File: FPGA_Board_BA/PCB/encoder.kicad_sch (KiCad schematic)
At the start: 1 part, among them J1101 Molex_Mini_Fit_Jr_2x08pin

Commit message: Besprechung mit Leo
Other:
- note added: "3 Phasen kommen auch vom gleichen Stecker, muss man vllt noch ändern JST Xh oder VH könnte hier bequem sein oder s04b-xask JST"
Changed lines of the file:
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@@
 	(generator_version "9.0")
 	(paper "A4")
+	(text "3 Phasen kommen auch vom gleichen Stecker, muss man vllt noch ändern\nJST Xh oder VH könnte hier bequem sein\noder s04b-xask JST"
+		(exclude_from_sim no)
+		(at 185.928 35.814 0)
+		(effects
+			(font
+				(size 1.27 1.27)
+			)
+			(justify left)
+		)
+	)
 	(text "(The encoder is not Differential)"
 		(exclude_from_sim no)

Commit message: lots of work
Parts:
- removed J1101: Molex_Mini_Fit_Jr_2x08pin, MYLIB_Misc:Molex_2x8pin_vertical_tht, symbol MYLIB_Misc:Molex_Mini_Fit_Jr_2x08
- added C1806, C1807, C1808, C1809: 100n_0603, WLIB_Capacitor:C_0603, symbol WLIB_C:100n_0603
- added J1801: Molex_Mini_Fit_Jr_2x08pin, MYLIB_Misc:Molex_2x8pin_vertical_tht, symbol MYLIB_Misc:Molex_Mini_Fit_Jr_2x08
- added U1802, U1803: SN74LXC2T45Q1, MYLIB_Misc:SN74LXC2T45QDCURQ1, symbol MYLIB_Misc:SN74LXC2T45Q1
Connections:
- net +5V: now also C1807.2, C1808.2, J1801.12 (Pin_12), U1802.1 (VCCA), U1802.5 (DIR), U1803.1 (VCCA), U1803.5 (DIR)
- net ENC_A: now also U1802.7 (B1)
- net ENC_B: now also U1802.6 (B2)
- net ENC_I: now also U1803.7 (B1)
- net GND: now also C1806.2, C1807.1, C1808.1, C1809.2, J1801.7 (Pin_7), U1802.4 (GND), U1803.4 (GND)
- new net +3.3V: C1806.1, C1809.1, U1802.8 (VCCB), U1803.8 (VCCB)
- new net ENC_A_5V: J1801.15 (Pin_15), U1802.2 (A1)
- new net ENC_B_5V: J1801.14 (Pin_14), U1802.3 (A2)
- new net ENC_I_5V: J1801.13 (Pin_13), U1803.2 (A1)
- new net M_PHA: J1801.9 (Pin_9)
- new net M_PHB: J1801.10 (Pin_10)
- new net M_PHC: J1801.11 (Pin_11)
- no-connect marks 11 -> 10

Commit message: work
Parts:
- renumbered C1808 to C72, C1807 to C73, C1809 to C74, C1806 to C75, J1801 to J20, U1802 to U16, U1803 to U17
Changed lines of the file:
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@@
 		(dnp no)
 		(fields_autoplaced yes)
-		(property "Reference" "#PWR01815"
+		(property "Reference" "#PWR099"
 			(at 251.46 130.81 0)
 			(effects
@@
 			(project "FPGA_Board_BA"
 				(path "/fd7503bc-e7fc-4766-b224-3d1c3d7de5ff/81c9b981-9c9c-474d-998d-986f60c2f16d"
-					(reference "#PWR01815")
+					(reference "#PWR099")
 					(unit 1)
 				)
@@
 		(dnp no)
 		(fields_autoplaced yes)
-		(property "Reference" "#PWR01817"
+		(property "Reference" "#PWR0100"
 			(at 254 87.63 0)
 			(effects
@@
 			(project "FPGA_Board_BA"
 				(path "/fd7503bc-e7fc-4766-b224-3d1c3d7de5ff/81c9b981-9c9c-474d-998d-986f60c2f16d"
-					(reference "#PWR01817")
+					(reference "#PWR0100")
 					(unit 1)
 				)
@@
 		(dnp no)
 		(fields_autoplaced yes)
-		(property "Reference" "#PWR01813"
+		(property "Reference" "#PWR090"
 			(at 187.96 144.78 0)
 			(effects
@@
 			(project "FPGA_Board_BA"
 				(path "/fd7503bc-e7fc-4766-b224-3d1c3d7de5ff/81c9b981-9c9c-474d-998d-986f60c2f16d"
-					(reference "#PWR01813")
+					(reference "#PWR090")
 					(unit 1)
 				)
@@
 		(dnp no)
 		(fields_autoplaced yes)
-		(property "Reference" "U1802"
+		(property "Reference" "U16"
 			(at 221.8533 104.14 0)
 			(effects
@@
 			(project ""
 				(path "/fd7503bc-e7fc-4766-b224-3d1c3d7de5ff/81c9b981-9c9c-474d-998d-986f60c2f16d"
-					(reference "U1802")
+					(reference "U16")
 					(unit 1)
 				)
@@
 		(dnp no)
 		(fields_autoplaced yes)
-		(property "Reference" "#PWR01808"
+		(property "Reference" "#PWR095"
 			(at 219.71 113.03 0)
 			(effects
@@
 			(project ""
 				(path "/fd7503bc-e7fc-4766-b224-3d1c3d7de5ff/81c9b981-9c9c-474d-998d-986f60c2f16d"
-					(reference "#PWR01808")
+					(reference "#PWR095")
 					(unit 1)
 				)
@@
 		(dnp no)
 		(fields_autoplaced yes)
-		(property "Reference" "C1806"
+		(property "Reference" "C75"
 			(at 243.84 111.76 90)
 			(effects
@@
 			(project ""
 				(path "/fd7503bc-e7fc-4766-b224-3d1c3d7de5ff/81c9b981-9c9c-474d-998d-986f60c2f16d"
-					(reference "C1806")
+					(reference "C75")
 					(unit 1)
 				)
@@
 		(dnp no)
 		(fields_autoplaced yes)
-		(property "Reference" "#PWR01816"
+		(property "Reference" "#PWR089"
 			(at 187.96 86.36 0)
 			(effects
@@
 			(project "FPGA_Board_BA"
 				(path "/fd7503bc-e7fc-4766-b224-3d1c3d7de5ff/81c9b981-9c9c-474d-998d-986f60c2f16d"
-					(reference "#PWR01816")
+					(reference "#PWR089")
 					(unit 1)
 				)
@@
 		(dnp no)
 		(fields_autoplaced yes)
-		(property "Reference" "U1803"
+		(property "Reference" "U17"
 			(at 221.8533 147.32 0)
 			(effects
@@
 			(project "FPGA_Board_BA"
 				(path "/fd7503bc-e7fc-4766-b224-3d1c3d7de5ff/81c9b981-9c9c-474d-998d-986f60c2f16d"
-					(reference "U1803")
+					(reference "U17")
 					(unit 1)
 				)
@@
 		(dnp no)
 		(fields_autoplaced yes)
-		(property "Reference" "#PWR01812"
+		(property "Reference" "#PWR091"
 			(at 189.23 100.33 0)
 			(effects
@@
 			(project "FPGA_Board_BA"
 				(path "/fd7503bc-e7fc-4766-b224-3d1c3d7de5ff/81c9b981-9c9c-474d-998d-986f60c2f16d"
-					(reference "#PWR01812")
+					(reference "#PWR091")
 					(unit 1)
 				)
@@
 		(dnp no)
 		(fields_autoplaced yes)
-		(property "Reference" "#PWR01814"
+		(property "Reference" "#PWR092"
 			(at 190.5 129.54 0)
 			(effects
@@
 			(project "FPGA_Board_BA"
 				(path "/fd7503bc-e7fc-4766-b224-3d1c3d7de5ff/81c9b981-9c9c-474d-998d-986f60c2f16d"
-					(reference "#PWR01814")
+					(reference "#PWR092")
 					(unit 1)
 				)
@@
 		(dnp no)
 		(fields_autoplaced yes)
-		(property "Reference" "J1801"
+		(property "Reference" "J20"
 			(at 220.98 30.48 0)
 			(effects
@@
 			(project ""
 				(path "/fd7503bc-e7fc-4766-b224-3d1c3d7de5ff/81c9b981-9c9c-474d-998d-986f60c2f16d"
-					(reference "J1801")
+					(reference "J20")
 					(unit 1)
 				)
@@
 		(dnp no)
 		(fields_autoplaced yes)
-		(property "Reference" "#PWR01810"
+		(property "Reference" "#PWR096"
 			(at 219.71 157.48 0)
 			(effects
@@
 			(project "FPGA_Board_BA"
 				(path "/fd7503bc-e7fc-4766-b224-3d1c3d7de5ff/81c9b981-9c9c-474d-998d-986f60c2f16d"
-					(reference "#PWR01810")
+					(reference "#PWR096")
 					(unit 1)
 				)
@@
 		(dnp no)
 		(fields_autoplaced yes)
-		(property "Reference" "#PWR01811"
+		(property "Reference" "#PWR097"
 			(at 226.06 121.92 0)
 			(effects
@@
 			(project "FPGA_Board_BA"
 				(path "/fd7503bc-e7fc-4766-b224-3d1c3d7de5ff/81c9b981-9c9c-474d-998d-986f60c2f16d"
-					(reference "#PWR01811")
+					(reference "#PWR097")
 					(unit 1)
 				)
@@
 		(dnp no)
 		(fields_autoplaced yes)
-		(property "Reference" "C1807"
+		(property "Reference" "C73"
 			(at 199.39 111.76 90)
 			(effects
@@
 			(project "FPGA_Board_BA"
 				(path "/fd7503bc-e7fc-4766-b224-3d1c3d7de5ff/81c9b981-9c9c-474d-998d-986f60c2f16d"
-					(reference "C1807")
+					(reference "C73")
 					(unit 1)
 				)
@@
 		(dnp no)
 		(fields_autoplaced yes)
-		(property "Reference" "#PWR01806"
+		(property "Reference" "#PWR093"
 			(at 210.82 78.74 0)
 			(effects
@@
 			(project "FPGA_Board_BA"
 				(path "/fd7503bc-e7fc-4766-b224-3d1c3d7de5ff/81c9b981-9c9c-474d-998d-986f60c2f16d"
-					(reference "#PWR01806")
+					(reference "#PWR093")
 					(unit 1)
 				)
@@
 		(dnp no)
 		(fields_autoplaced yes)
-		(property "Reference" "C1808"
+		(property "Reference" "C72"
 			(at 198.12 68.58 90)
 			(effects
@@
 			(project "FPGA_Board_BA"
 				(path "/fd7503bc-e7fc-4766-b224-3d1c3d7de5ff/81c9b981-9c9c-474d-998d-986f60c2f16d"
-					(reference "C1808")
+					(reference "C72")
 					(unit 1)
 				)
@@
 		(dnp no)
 		(fields_autoplaced yes)
-		(property "Reference" "#PWR01807"
+		(property "Reference" "#PWR098"
 			(at 228.6 78.74 0)
 			(effects
@@
 			(project ""
 				(path "/fd7503bc-e7fc-4766-b224-3d1c3d7de5ff/81c9b981-9c9c-474d-998d-986f60c2f16d"
-					(reference "#PWR01807")
+					(reference "#PWR098")
 					(unit 1)
 				)
@@
 		(dnp no)
 		(fields_autoplaced yes)
-		(property "Reference" "#PWR01809"
+		(property "Reference" "#PWR094"
 			(at 213.36 121.92 0)
 			(effects
@@
 			(project "FPGA_Board_BA"
 				(path "/fd7503bc-e7fc-4766-b224-3d1c3d7de5ff/81c9b981-9c9c-474d-998d-986f60c2f16d"
-					(reference "#PWR01809")
+					(reference "#PWR094")
 					(unit 1)
 				)
@@
 		(dnp no)
 		(fields_autoplaced yes)
-		(property "Reference" "C1809"
+		(property "Reference" "C74"
 			(at 241.3 68.58 90)
 			(effects
@@
 			(project "FPGA_Board_BA"
 				(path "/fd7503bc-e7fc-4766-b224-3d1c3d7de5ff/81c9b981-9c9c-474d-998d-986f60c2f16d"
-					(reference "C1809")
-					(unit 1)
-				)
+					(reference "C74")
+					(unit 1)
+				)

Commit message: Besprechung mit Leo
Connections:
- net M_PHA: no longer names the net of J20.9 (Pin_9)
- net M_PHB: no longer names the net of J20.10 (Pin_10)
- net M_PHC: no longer names the net of J20.11 (Pin_11)
- no-connect marks 10 -> 13
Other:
- note added: "JST 6 pin für Encoder"
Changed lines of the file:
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@@
 		)
 	)
+	(text "JST 6 pin für Encoder"
+		(exclude_from_sim no)
+		(at 253.492 24.13 0)
+		(effects
+			(font
+				(size 1.27 1.27)
+			)
+		)
+	)
 	(junction
 		(at 219.71 149.86)
@@
 	)
 	(no_connect
+		(at 227.33 36.83)
+	)
+	(no_connect
 		(at 214.63 46.99)
 	)
@@
 	)
 	(no_connect
+		(at 227.33 41.91)
+	)
+	(no_connect
 		(at 229.87 137.16)
 	)
@@
 	)
 	(no_connect
+		(at 227.33 39.37)
+	)
+	(no_connect
 		(at 214.63 36.83)
 	)
@@
 	(wire
 		(pts
-			(xy 227.33 41.91) (xy 233.68 41.91)
-		)
-		(stroke
-			(width 0)
-			(type default)
-		)
-	)
-	(wire
-		(pts
 			(xy 209.55 142.24) (xy 187.96 142.24)
 		)
@@
 	(wire
 		(pts
-			(xy 227.33 36.83) (xy 233.68 36.83)
-		)
-		(stroke
-			(width 0)
-			(type default)
-		)
-	)
-	(wire
-		(pts
 			(xy 217.17 119.38) (xy 217.17 121.92)
 		)
@@
 	(wire
 		(pts
-			(xy 227.33 39.37) (xy 233.68 39.37)
-		)
-		(stroke
-			(width 0)
-			(type default)
-		)
-	)
-	(wire
-		(pts
 			(xy 238.76 52.07) (xy 227.33 52.07)
 		)
@@
 		)
 	)
-	(global_label "M_PHC"
-		(shape bidirectional)
-		(at 233.68 41.91 0)
-		(fields_autoplaced yes)
-		(effects
-			(font
-				(size 1.27 1.27)
-			)
-			(justify left)
-		)
-		(property "Intersheetrefs" "${INTERSHEET_REFS}"
-			(at 244.066 41.91 0)
-			(effects
-				(font
-					(size 1.27 1.27)
-				)
-				(justify left)
-				(hide yes)
-			)
-		)
-	)
-	(global_label "M_PHB"
-		(shape bidirectional)
-		(at 233.68 39.37 0)
-		(fields_autoplaced yes)
-		(effects
-			(font
-				(size 1.27 1.27)
-			)
-			(justify left)
-		)
-		(property "Intersheetrefs" "${INTERSHEET_REFS}"
-			(at 244.066 39.37 0)
-			(effects
-				(font
-					(size 1.27 1.27)
-				)
-				(justify left)
-				(hide yes)
-			)
-		)
-	)
-	(global_label "M_PHA"
-		(shape bidirectional)
-		(at 233.68 36.83 0)
-		(fields_autoplaced yes)
-		(effects
-			(font
-				(size 1.27 1.27)
-			)
-			(justify left)
-		)
-		(property "Intersheetrefs" "${INTERSHEET_REFS}"
-			(at 243.8846 36.83 0)
-			(effects
-				(font
-					(size 1.27 1.27)
-				)
-				(justify left)
-				(hide yes)
-			)
-		)
-	)

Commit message: 22.11
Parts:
- removed C72, C73, C74, C75: 100n_0603, WLIB_Capacitor:C_0603, symbol WLIB_C:100n_0603
- removed J20: Molex_Mini_Fit_Jr_2x08pin, MYLIB_Misc:Molex_2x8pin_vertical_tht, symbol MYLIB_Misc:Molex_Mini_Fit_Jr_2x08
- removed U16, U17: SN74LXC2T45Q1, MYLIB_Misc:SN74LXC2T45QDCURQ1, symbol MYLIB_Misc:SN74LXC2T45Q1
- added J20: JST_XH_05_vertical, Connector_JST:JST_XH_B5B-XH-A_1x05_P2.50mm_Vertical, symbol WLIB_J:JST_XH_05_vertical
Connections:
- net +5V: now also J20.1 (Pin_1)
- net ENC_A_5V: now also J20.5 (Pin_5)
- net ENC_B_5V: now also J20.4 (Pin_4)
- net ENC_I_5V: now also J20.3 (Pin_3)
- net GND: now also J20.2 (Pin_2)
- no-connect marks 13 -> 2
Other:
- added sheet Level Shifter Encoder 1 (ls_encoder.kicad_sch)
- added sheet Level Shifter Encoder 2 (ls_encoder.kicad_sch)
- note added: "JST 5 pin für Encoder"
- note removed: "3 Phasen kommen auch vom gleichen Stecker, muss man vllt noch ändern JST Xh oder VH könnte hier bequem sein oder s04b-xask JST"
- note removed: "JST 6 pin für Encoder"

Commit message: exported stuff
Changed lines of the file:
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@@
 	(rectangle
 		(start 194.31 26.67)
-		(end 247.65 55.88)
+		(end 257.81 55.88)
 		(stroke
 			(width 0)
@@
 		)
 	)
+	(junction
+		(at 231.14 38.1)
+		(diameter 0)
+		(color 0 0 0 0)
+	)
 	(no_connect
 		(at 238.76 102.87)
@@
 	(wire
 		(pts
+			(xy 247.65 41.91) (xy 247.65 40.64)
+		)
+		(stroke
+			(width 0)
+			(type default)
+		)
+	)
+	(wire
+		(pts
 			(xy 190.5 100.33) (xy 209.55 100.33)
 		)
@@
 	(wire
 		(pts
-			(xy 234.95 102.87) (xy 238.76 102.87)
+			(xy 247.65 40.64) (xy 224.79 40.64)
 		)
 		(stroke
@@
 	(wire
 		(pts
-			(xy 224.79 40.64) (xy 238.76 40.64)
+			(xy 234.95 102.87) (xy 238.76 102.87)
 		)
 		(stroke
@@
 	(wire
 		(pts
-			(xy 224.79 38.1) (xy 238.76 38.1)
+			(xy 224.79 38.1) (xy 231.14 38.1)
 		)
 		(stroke
@@
 	(wire
 		(pts
+			(xy 231.14 38.1) (xy 238.76 38.1)
+		)
+		(stroke
+			(width 0)
+			(type default)
+		)
+	)
+	(wire
+		(pts
 			(xy 194.31 85.09) (xy 209.55 85.09)
 		)
@@
 		)
 	)
+	(wire
+		(pts
+			(xy 231.14 34.29) (xy 231.14 38.1)
+		)
+		(stroke
+			(width 0)
+			(type default)
+		)
+	)
 	(image
 		(at 91.44 64.3793)
@@
 	)
 	(symbol
+		(lib_id "power:GND")
+		(at 247.65 41.91 0)
+		(unit 1)
+		(exclude_from_sim no)
+		(in_bom yes)
+		(on_board yes)
+		(dnp no)
+		(fields_autoplaced yes)
+		(property "Reference" "#PWR0285"
+			(at 247.65 48.26 0)
+			(effects
+				(font
+					(size 1.27 1.27)
+				)
+				(hide yes)
+			)
+		)
+		(property "Value" "GND"
+			(at 247.65 46.99 0)
+			(effects
+				(font
+					(size 1.27 1.27)
+				)
+			)
+		)
+		(property "Footprint" ""
+			(at 247.65 41.91 0)
+			(effects
+				(font
+					(size 1.27 1.27)
+				)
+				(hide yes)
+			)
+		)
+		(property "Datasheet" ""
+			(at 247.65 41.91 0)
+			(effects
+				(font
+					(size 1.27 1.27)
+				)
+				(hide yes)
+			)
+		)
+		(property "Description" "Power symbol creates a global label with name \"GND\" , ground"
+			(at 247.65 41.91 0)
+			(effects
+				(font
+					(size 1.27 1.27)
+				)
+				(hide yes)
+			)
+		)
+		(pin "1"
+		)
+		(instances
+			(project ""
+				(path "/fd7503bc-e7fc-4766-b224-3d1c3d7de5ff/81c9b981-9c9c-474d-998d-986f60c2f16d"
+					(reference "#PWR0285")
+					(unit 1)
+				)
+			)
+		)
+	)
+	(symbol
 		(lib_id "WLIB_J:JST_XH_05_vertical")
 		(at 219.71 43.18 0)
@@
 					(unit 1)
 				)
+			)
+		)
+	)
+	(symbol
+		(lib_id "power:+5V")
+		(at 231.14 34.29 0)
+		(unit 1)
+		(exclude_from_sim no)
+		(in_bom yes)
+		(on_board yes)
+		(dnp no)
+		(fields_autoplaced yes)
+		(property "Reference" "#PWR0284"
+			(at 231.14 38.1 0)
+			(effects
+				(font
+					(size 1.27 1.27)
+				)
+				(hide yes)
+			)
+		)
+		(property "Value" "+5V"
+			(at 231.14 29.21 0)
+			(effects
+				(font
+					(size 1.27 1.27)
+				)
+			)
+		)
+		(property "Footprint" ""
+			(at 231.14 34.29 0)
+			(effects
+				(font
+					(size 1.27 1.27)
+				)
+				(hide yes)
+			)
+		)
+		(property "Datasheet" ""
+			(at 231.14 34.29 0)
+			(effects
+				(font
+					(size 1.27 1.27)
+				)
+				(hide yes)
+			)
+		)
+		(property "Description" "Power symbol creates a global label with name \"+5V\""
+			(at 231.14 34.29 0)
+			(effects
+				(font
+					(size 1.27 1.27)
+				)
+				(hide yes)
+			)
+		)
+		(pin "1"
+		)
+		(instances
+			(project ""
+				(path "/fd7503bc-e7fc-4766-b224-3d1c3d7de5ff/81c9b981-9c9c-474d-998d-986f60c2f16d"
+					(reference "#PWR0284")
+					(unit 1)
+				)

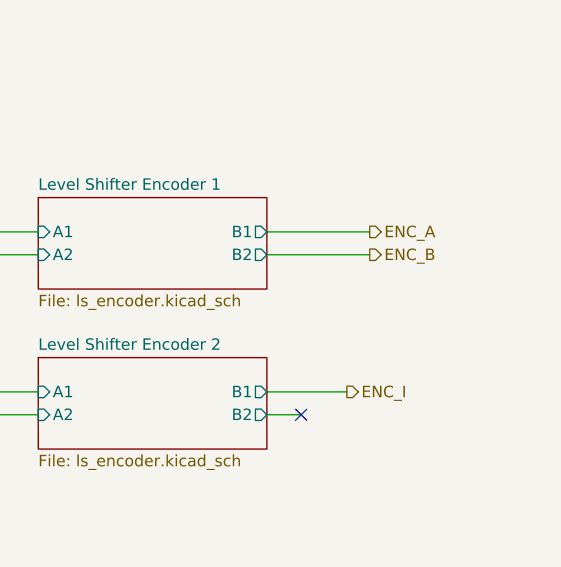
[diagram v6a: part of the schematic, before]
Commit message: big schematic cleanup. Added wire to bus
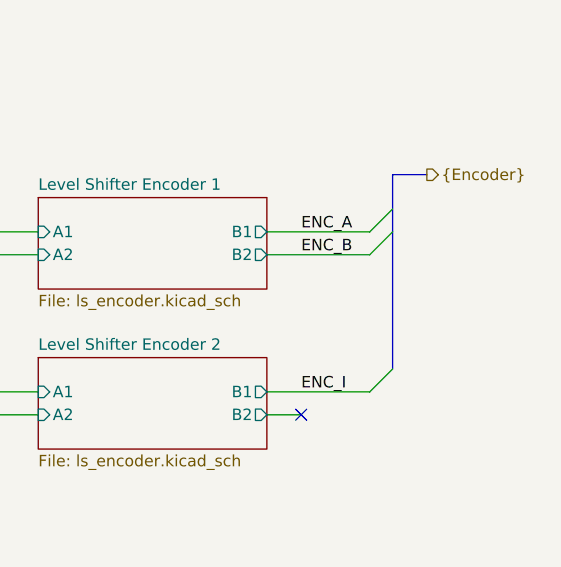
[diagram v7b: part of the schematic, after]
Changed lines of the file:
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@@
 		(at 204.47 102.87)
 	)
+	(bus_entry
+		(at 246.38 85.09)
+		(size 2.54 -2.54)
+		(stroke
+			(width 0)
+			(type default)
+		)
+	)
+	(bus_entry
+		(at 246.38 100.33)
+		(size 2.54 -2.54)
+		(stroke
+			(width 0)
+			(type default)
+		)
+	)
+	(bus_entry
+		(at 246.38 82.55)
+		(size 2.54 -2.54)
+		(stroke
+			(width 0)
+			(type default)
+		)
+	)
 	(wire
 		(pts
@@
 	(wire
 		(pts
-			(xy 234.95 100.33) (xy 243.84 100.33)
+			(xy 234.95 100.33) (xy 246.38 100.33)
 		)
 		(stroke
@@
 		)
 	)
+	(bus
+		(pts
+			(xy 248.92 82.55) (xy 248.92 80.01)
+		)
+		(stroke
+			(width 0)
+			(type default)
+		)
+	)
+	(bus
+		(pts
+			(xy 248.92 76.2) (xy 252.73 76.2)
+		)
+		(stroke
+			(width 0)
+			(type default)
+		)
+	)
 	(wire
 		(pts
@@
 		)
 	)
+	(bus
+		(pts
+			(xy 248.92 80.01) (xy 248.92 76.2)
+		)
+		(stroke
+			(width 0)
+			(type default)
+		)
+	)
 	(wire
 		(pts
@@
 		)
 	)
+	(bus
+		(pts
+			(xy 248.92 97.79) (xy 248.92 82.55)
+		)
+		(stroke
+			(width 0)
+			(type default)
+		)
+	)
 	(image
 		(at 91.44 64.3793)
@@
 		)
 	)
+	(label "ENC_B"
+		(at 238.76 85.09 0)
+		(effects
+			(font
+				(size 1.27 1.27)
+			)
+			(justify left bottom)
+		)
+	)
+	(label "ENC_I"
+		(at 238.76 100.33 0)
+		(effects
+			(font
+				(size 1.27 1.27)
+			)
+			(justify left bottom)
+		)
+	)
 	(label "ENC_A_5V"
 		(at 238.76 48.26 180)
@@
 		)
 	)
-	(label "ENC_B_5V"
-		(at 238.76 45.72 180)
-		(effects
-			(font
-				(size 1.27 1.27)
-			)
-			(justify right bottom)
-		)
-	)
-	(label "ENC_A_5V"
-		(at 194.31 82.55 0)
+	(label "ENC_A"
+		(at 238.76 82.55 0)
 		(effects
 			(font
@@
 		)
 	)
-	(hierarchical_label "ENC_A"
-		(shape output)
-		(at 246.38 82.55 0)
+	(label "ENC_B_5V"
+		(at 238.76 45.72 180)
 		(effects
 			(font
 				(size 1.27 1.27)
 			)
-			(justify left)
+			(justify right bottom)
 		)
 	)
-	(hierarchical_label "ENC_B"
-		(shape output)
-		(at 246.38 85.09 0)
+	(label "ENC_A_5V"
+		(at 194.31 82.55 0)
 		(effects
 			(font
 				(size 1.27 1.27)
 			)
-			(justify left)
+			(justify left bottom)
 		)
 	)
-	(hierarchical_label "ENC_I"
+	(hierarchical_label "{Encoder}"
 		(shape output)
-		(at 243.84 100.33 0)
+		(at 252.73 76.2 0)
 		(effects
 			(font
